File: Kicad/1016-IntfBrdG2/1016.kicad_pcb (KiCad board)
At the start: 2 copper layers, 43.2 x 12.7 mm, 10 parts, among them P1 TST, P2 CONN_4, P3 CONN_4, P4 CONN_4, P5 CONN_4X2, P6 CONN_4X2, P7 CONN_4

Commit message: Updates to silkscreen and created mashup.  These Gerbers sent to PCB house.
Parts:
- R1: value 100K -> 0
- moved P4 40.7 mm to (201.9, 177.8), turned to 270 degrees
- moved P2 34.5 mm to (165.1, 181.6), turned to 0 degrees
- moved P3 34.5 mm to (165.1, 171.4), turned to 0 degrees
- moved R1 33.0 mm to (165.1, 176.5), turned to 180 degrees
- moved P1 32.7 mm to (197.5, 172.7), turned to 180 degrees
- moved R2 32.4 mm to (197.5, 179.7), turned to 0 degrees
- moved R3 31.8 mm to (197.5, 176.5), turned to 0 degrees
- moved P5 17.0 mm to (189.2, 180.3), turned to 0 degrees
- moved P6 17.0 mm to (189.2, 172.7), turned to 0 degrees
- moved P7 11.5 mm to (175.9, 177.2), turned to 270 degrees
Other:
- board text added: "5v"
- board text added: "Gnd"
- board text added: "Rx"
- board text added: "Tx"

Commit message: Added OPP logo to all boards.  Better late than never.
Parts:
- added VAL: REF, opp_logo_backsilk, F.Cu at (181.6, 175.3)

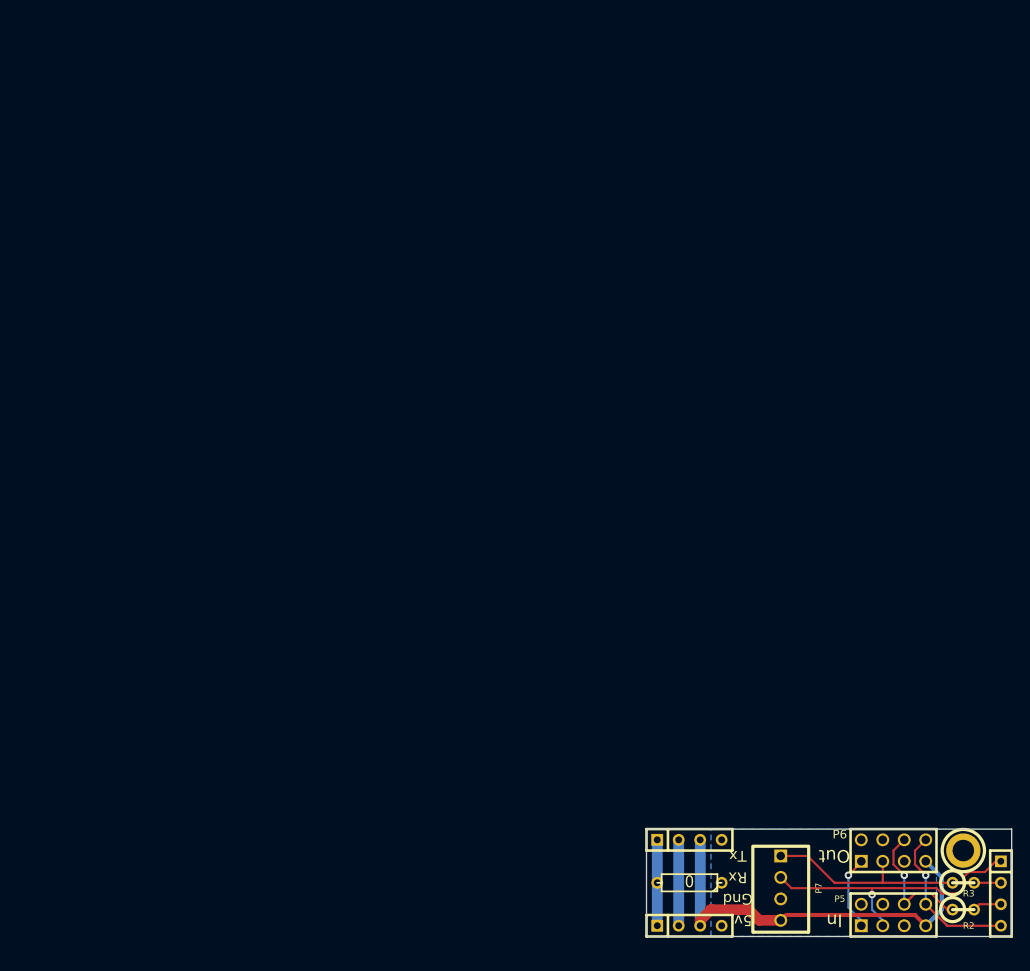
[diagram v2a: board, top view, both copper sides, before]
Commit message: Changed size of PCB sheets to 8.5" x 11".  Added name/rev/board name to PCB sheets.
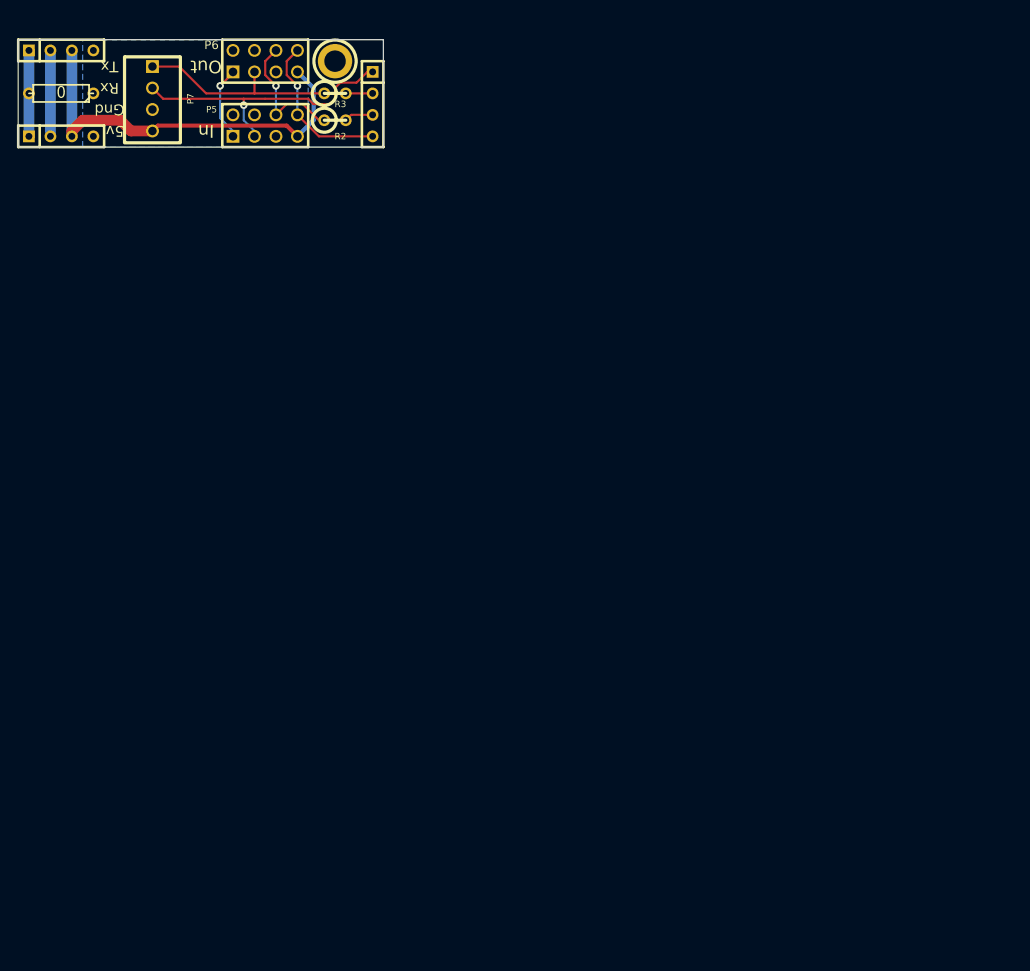
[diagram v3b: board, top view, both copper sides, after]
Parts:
- moved P1 119.3 mm to (123.2, 79.4)
- moved P4 119.3 mm to (127.6, 84.5)
- moved P7 119.3 mm to (101.6, 83.8)
- moved R2 119.3 mm to (123.2, 86.4)
- moved R3 119.3 mm to (123.2, 83.2)
- moved VAL 119.3 mm to (107.3, 81.9)
- moved P2 119.3 mm to (90.8, 88.3)
- moved P5 119.3 mm to (114.9, 87.0)
- moved P6 119.3 mm to (114.9, 79.4)
- moved R1 119.3 mm to (90.8, 83.2)
- moved P3 119.3 mm to (90.8, 78.1)

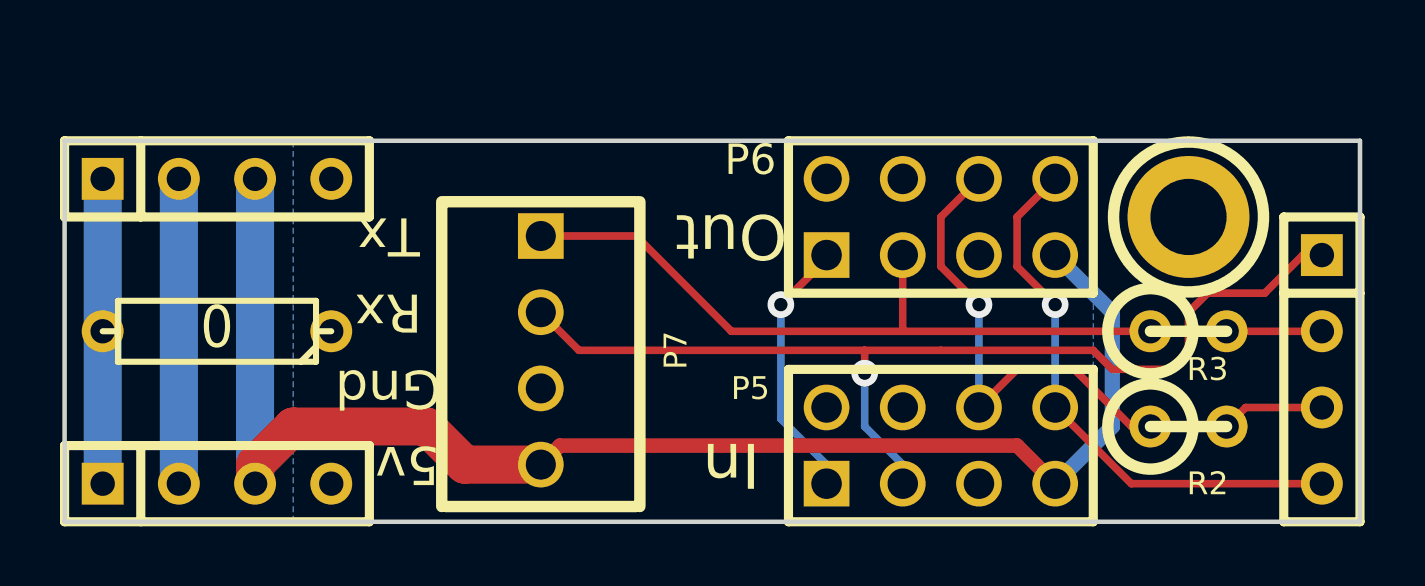
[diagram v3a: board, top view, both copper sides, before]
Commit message: Gen2 embedded code: Remove debug code that always overwrites NV configuration.  Added Gen2.rev0.1.1.0.cyacd for downloading to boards.
PopulateBrd document:
Correct solenoid pinout picture.

SolDrvG2 board:
Move location of 4 pin switch input header to reduce interference with interface board.  Update to use cheaper 6 pin Molex header.  Add rev to copper layer.

IntfBrdG2 board:
Change future pin on ribbon cable connector to carry 12V.  Make board slightly larger so it can be panellized by IteadStudio.  Add better grounding.  Move ribbon cable connectors so less interference with solenoid board input header.  Add 3 pin header to make communicating with first board in chain easier (switch comms between 4 pin header and ribbon cable).  Add rev to copper layer.

IncandSMG2 board:
Update to use cheaper 2 pin Molex header.  Add rev to copper layer.

Panellize Gerbers:
Add panellized boards for SolDrvG2, IntfBrdG2, and IncandSMG2.

MPF/SS3:
Small updates to add skillshot.
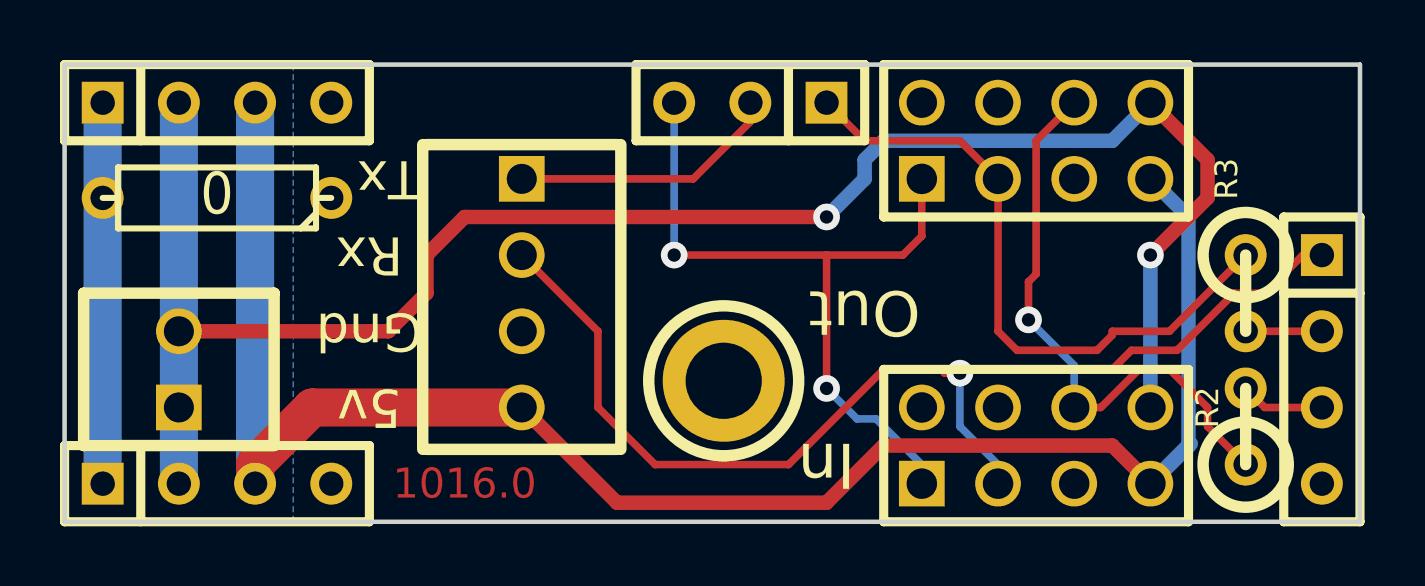
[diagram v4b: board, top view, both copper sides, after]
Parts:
- added P15: CONN_2, 00_th1x2x100-lock, F.Cu at (89.5, 84.5)
- added P8: CONN_3, SIL-3, F.Cu at (108.6, 75.6)
- moved P1 16.4 mm to (107.7, 84.8)
- moved VAL 9.55 mm to (97.8, 81.3), turned to 270 degrees
- moved R1 4.45 mm to (90.8, 78.7)
- moved P6 4.07 mm to (118.1, 76.8)
- moved P5 3.17 mm to (118.1, 87.0)
- moved P3 2.54 mm to (90.8, 75.6)
- moved R3 2.29 mm to (125.1, 81.9), turned to 270 degrees
- moved P7 2.01 mm to (101.0, 81.9)
- moved R2 1.91 mm to (125.1, 86.4), turned to 90 degrees
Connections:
- P4 pad 4: /FUTURE -> (no net)
- P5 pad 8: /FUTURE -> +12V1
- P6 pad 3: N-000009 -> N-000002
- P6 pad 8: /FUTURE -> +12V1
- P7 pad 1: N-000009 -> N-000007
- R3 pad 1: N-000009 -> N-000002
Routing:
- net +12V1: track 10.2 -> 61.1 mm, vias 0 -> 2
- net N-000009: track 24.2 -> 0.00 mm
- net N-000002: track 0.00 -> 21.8 mm
- net /FUTURE: track 18.6 -> 0.00 mm, vias 1 -> 0
- net N-000008: track 8.88 -> 24.8 mm, vias 1 -> 2
- net +5V: track 48.5 -> 58.5 mm
- net N-000007: track 0.00 -> 9.04 mm
- net /P0: track 34.1 -> 38.3 mm
- net N-0000011: track 15.7 -> 19.4 mm
- net GNDPWR: track 10.2 -> 12.7 mm
- net /P2: track 3.44 -> 2.80 mm
- net /P1: track 3.18 -> 2.54 mm
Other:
- board size 43.2 x 12.7 mm -> 43.2 x 15.2 mm
- board text added: "1016.0"
